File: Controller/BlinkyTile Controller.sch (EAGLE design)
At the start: 27 parts, among them IC1 74LVC1G17DCK, IC2 74LVC1G17DCK, Q1 CRYSTAL_4PAD2520, SW1 SPST_TACT-EVQQ2, SW2 SPST_TACT-EVQQ2, T1 TEST_PAD-7, T2 TEST_PAD-7, U1 MK20DX128VLF5

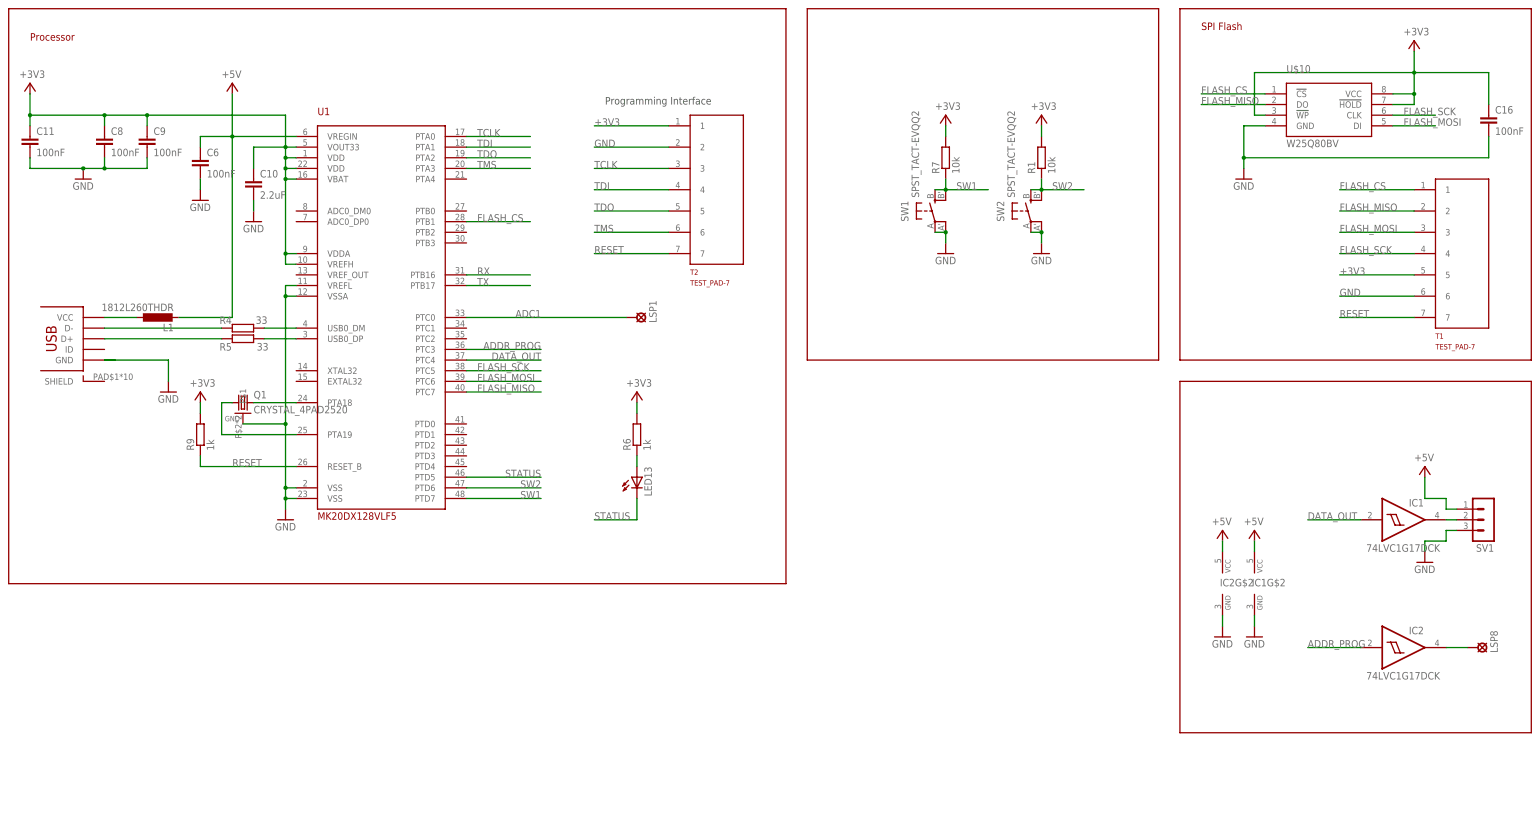
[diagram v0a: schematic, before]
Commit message: Update controller board design for RevA
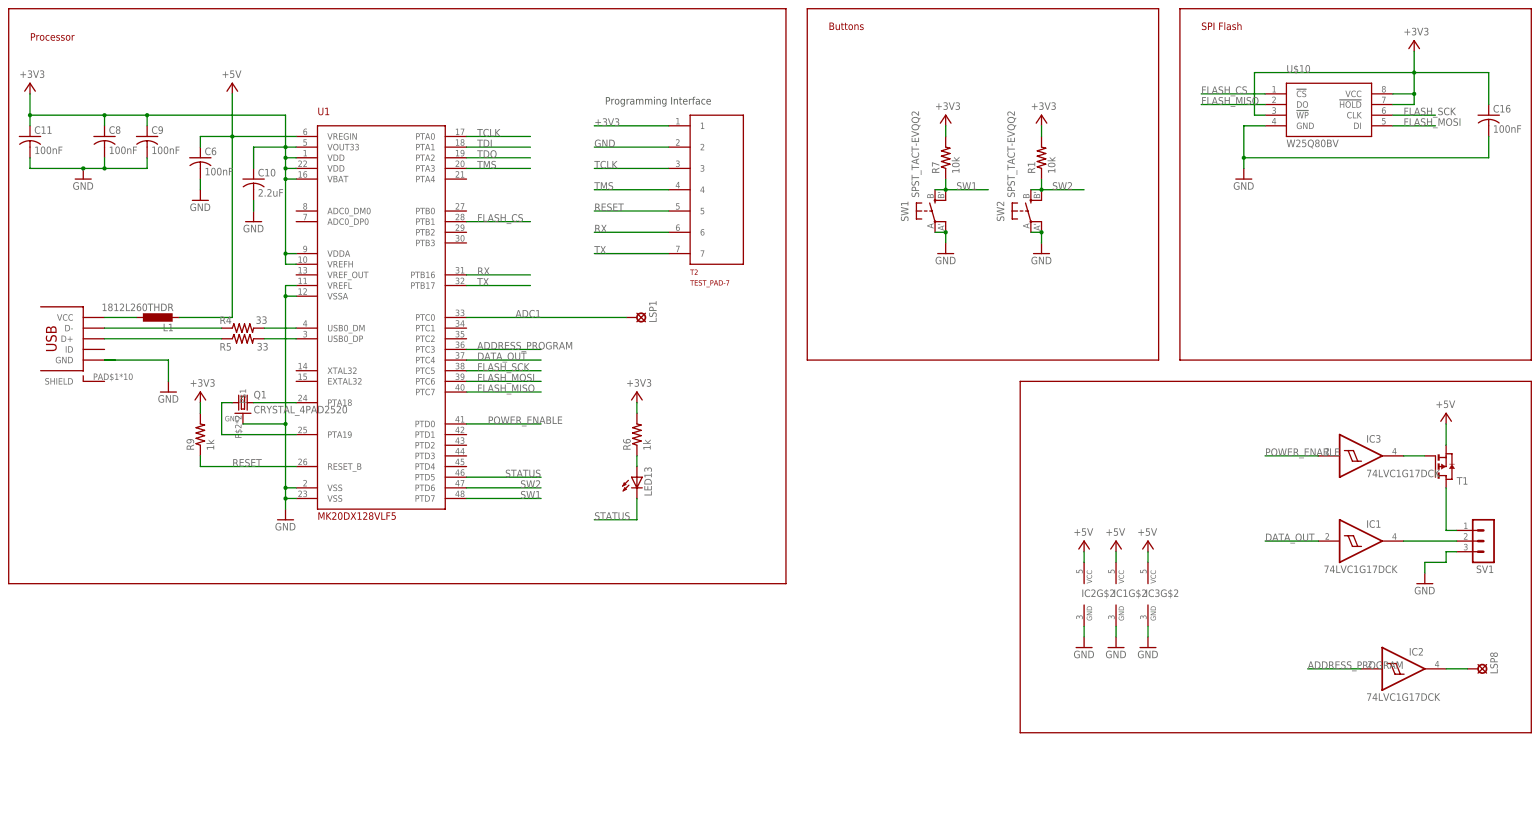
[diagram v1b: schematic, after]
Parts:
- added IC3: 74LVC1G17DCK, 74xx-little-us:74LVC1G17DCK
- C10, C11, C16, C6, C8, C9: device rcl:C-EUC0402 -> adafruit:C-USC0402
- R1, R4, R5, R6, R7, R9: device rcl:R-EU_R0402 -> adafruit:R-US_R0402
- T1: value TEST_PAD-7 -> (none); device Sam Library:TEST_PAD-7 -> zetex:PMOSSOT23
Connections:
- net ADDR_PROG renamed ADDRESS_PROGRAM
- new net N$5: SV1.1, T1.D
- new net N$6: IC3G$1.O, T1.G
- new net POWER_ENABLE: IC3G$1.I, U1.PTD0
- net +3V3: no longer T1.5
- net +5V: now also IC3G$2.VCC, T1.S; no longer SV1.1
- net FLASH_CS: no longer T1.1
- net FLASH_MISO: no longer T1.2
- net FLASH_MOSI: no longer T1.3
- net FLASH_SCK: no longer T1.4
- net GND: now also IC3G$2.GND; no longer T1.6
- net RESET: now also T2.5; no longer T1.7, T2.7
- net RX: now also T2.6
- net TDI: no longer T2.4
- net TDO: no longer T2.5
- net TMS: now also T2.4; no longer T2.6
- net TX: now also T2.7
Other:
- note added: "Buttons"
- moved on the sheet: IC1, IC1G$2, IC2, IC2G$2, LSP8, SV1

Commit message: Switch to smaller processor, change FLASH_CS to hardware CS pin
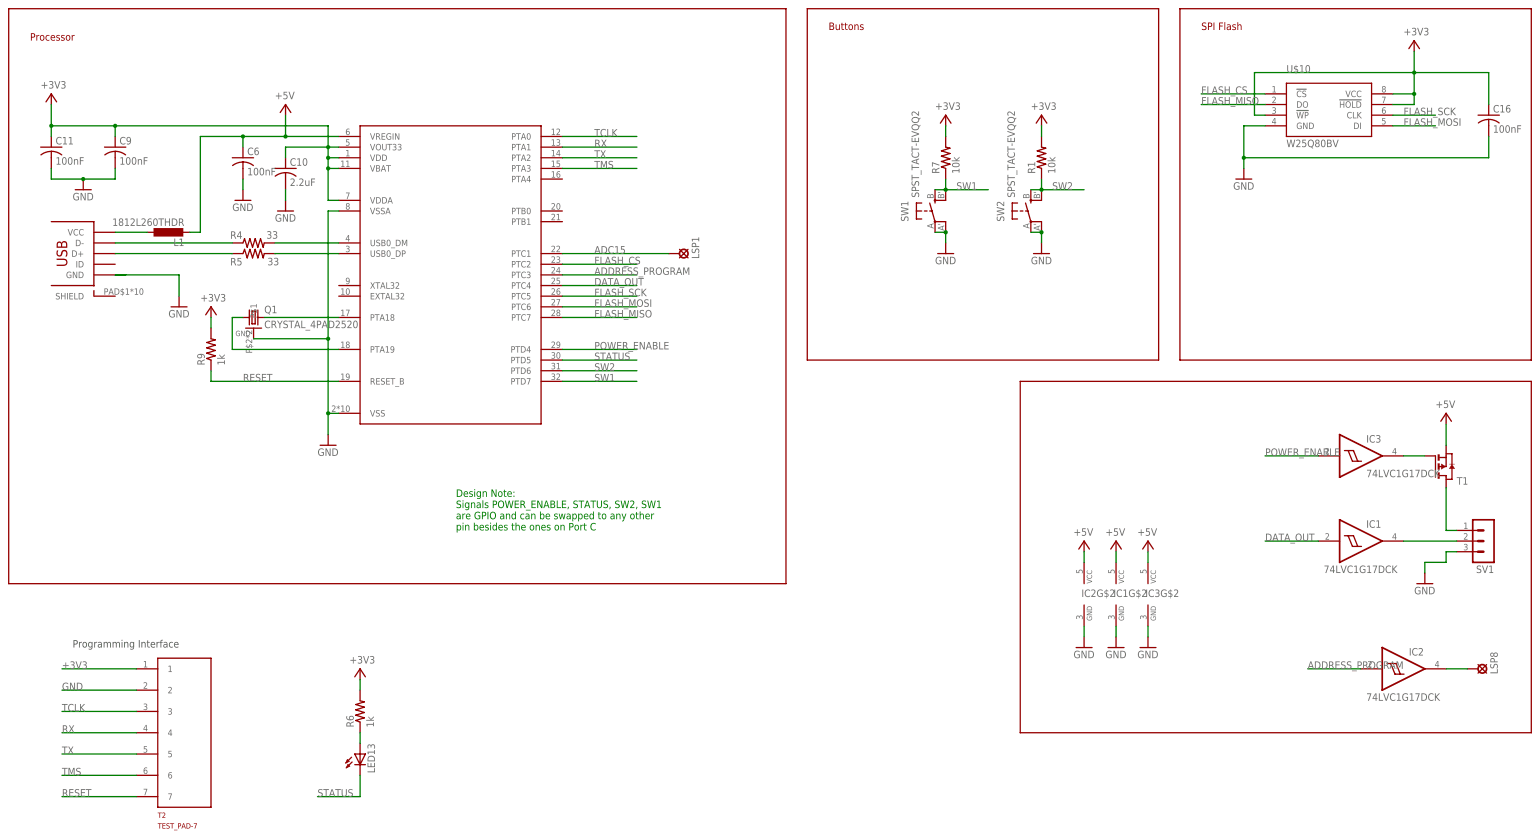
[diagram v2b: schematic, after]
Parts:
- removed C8: 100nF, adafruit:C-USC0402
- removed U1: MK20DX128VLF5, scanlime:MK20DX128VLF5
- added U$1: MK20D--VFM5, blinkinlabs:MK20D--VFM5
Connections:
- removed net ADC1: LSP1.MP, U1.PTC0
- removed net TDI: U1.PTA1
- removed net TDO: U1.PTA2
- new net ADC15: LSP1.MP, U$1.PTC1
- net +3V3: now also U$1.VBAT, U$1.VDD, U$1.VDDA, U$1.VOUT33; no longer C8.1, U1.VBAT, U1.VDD@1, U1.VDD@2, U1.VDDA, U1.VOUT33, U1.VREFH
- net +5V: now also U$1.VREGIN; no longer U1.VREGIN
- net ADDRESS_PROGRAM: now also U$1.PTC3; no longer U1.PTC3
- net DATA_OUT: now also U$1.PTC4; no longer U1.PTC4
- net FLASH_CS: now also U$1.PTC2; no longer U1.PTB1
- net FLASH_MISO: now also U$1.PTC7; no longer U1.PTC7
- net FLASH_MOSI: now also U$1.PTC6; no longer U1.PTC6
- net FLASH_SCK: now also U$1.PTC5; no longer U1.PTC5
- net GND: now also U$1.VSS, U$1.VSSA; no longer C8.2, U1.VREFL, U1.VSS@1, U1.VSS@2, U1.VSSA
- net N$1: now also U$1.PTA19; no longer U1.PTA19
- net N$11: now also U$1.USB0_DM; no longer U1.USB0_DM
- net N$12: now also U$1.USB0_DP; no longer U1.USB0_DP
- net N$2: now also U$1.PTA18; no longer U1.PTA18
- net POWER_ENABLE: now also U$1.PTD4; no longer U1.PTD0
- net RESET: now also T2.7, U$1.RESET_B; no longer T2.5, U1.RESET_B
- net RX: now also T2.4, U$1.PTA1; no longer T2.6, U1.PTB16
- net STATUS: now also U$1.PTD5; no longer U1.PTD5
- net SW1: now also U$1.PTD7; no longer U1.PTD7
- net SW2: now also U$1.PTD6; no longer U1.PTD6
- net TCLK: now also U$1.PTA0; no longer U1.PTA0
- net TMS: now also T2.6, U$1.PTA3; no longer T2.4, U1.PTA3
- net TX: now also T2.5, U$1.PTA2; no longer T2.7, U1.PTB17
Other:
- note added: "Design Note: Signals POWER_ENABLE, STATUS, SW2, SW1 are GPIO and can be swapped to any other pin besides the ones on Port C"
- moved on the sheet: C10, C11, C6, C9, L1, LED13, LSP1, Q1, R4, R5, R6, R9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

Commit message: Update to RevB controller from Sam
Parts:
- removed LED13: (no value), adafruit:LEDCHIPLED_0805
- removed R7: 10k, adafruit:R-US_R0402
- removed T2: TEST_PAD-7, Sam Library:TEST_PAD-7
- added C3: 100nF, adafruit:C-USC0402
- added CON2: F-2X04-DIL-100, con-headers-jp:F-2X04-DIL-100
- added LED1: STATUS, adafruit:LEDCHIPLED_0805
- added R2: 33, adafruit:R-US_R0402
- R1: value 10k -> 33
- R4: value 33 -> 1k
- R5: value 33 -> 10k
- R6: value 1k -> 10k
- TP1: value SE11 -> ADCIN
- TP2: value SE11 -> ADDRESS
- renumbered C10 to C4, C11 to C1, C16 to C5, C9 to C2, IC1 to U4, IC2 to U5, IC3 to U3, LSP1 to TP1, LSP8 to TP2, R9 to R3, SV1 to CON3, U$1 to U1, U$10 to U2, U$7 to CON1
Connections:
- new net PA4: CON2.8, U1.PTA4
- net +3V3: now also C6.1, CON2.1, R4.2, R5.2; no longer R1.2, R7.2, T2.1
- net +5V: now also C3.1; no longer C6.1
- net GND: now also C3.2, CON2.2; no longer T2.2
- net N$10: now also R2.1; no longer R5.1
- net N$11: now also R1.2; no longer R4.2
- net N$12: now also R2.2; no longer R5.2
- net N$16: now also LED1.A, R4.1; no longer LED13.A, R6.1
- net N$9: now also R1.1; no longer R4.1
- net RESET: now also CON2.7; no longer T2.7
- net RX: now also CON2.4; no longer T2.4
- net STATUS: now also LED1.C, U1.PTD7; no longer LED13.C, U1.PTD5
- net SW1: now also R5.1, U1.PTD6; no longer R7.1, U1.PTD7
- net SW2: now also R6.1, U1.PTD5; no longer R1.1, U1.PTD6
- net TCLK: now also CON2.3; no longer T2.3
- net TMS: now also CON2.6; no longer T2.6
- net TX: now also CON2.5; no longer T2.5
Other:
- moved on the sheet: C6, R1, R4, R5, R6

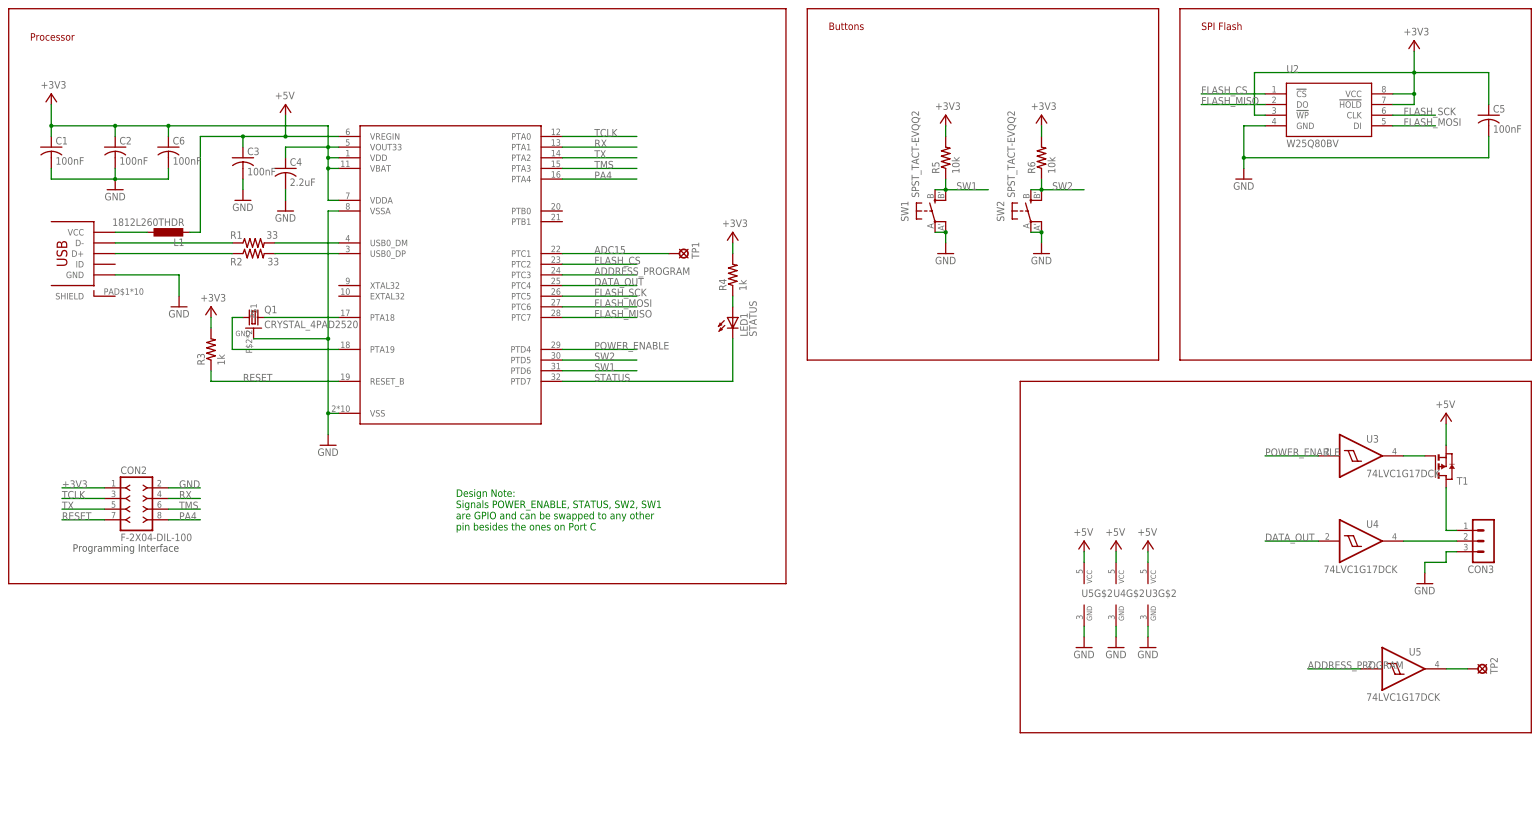
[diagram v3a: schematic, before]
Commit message: PCB updates: Drop pullup resistors, change connector
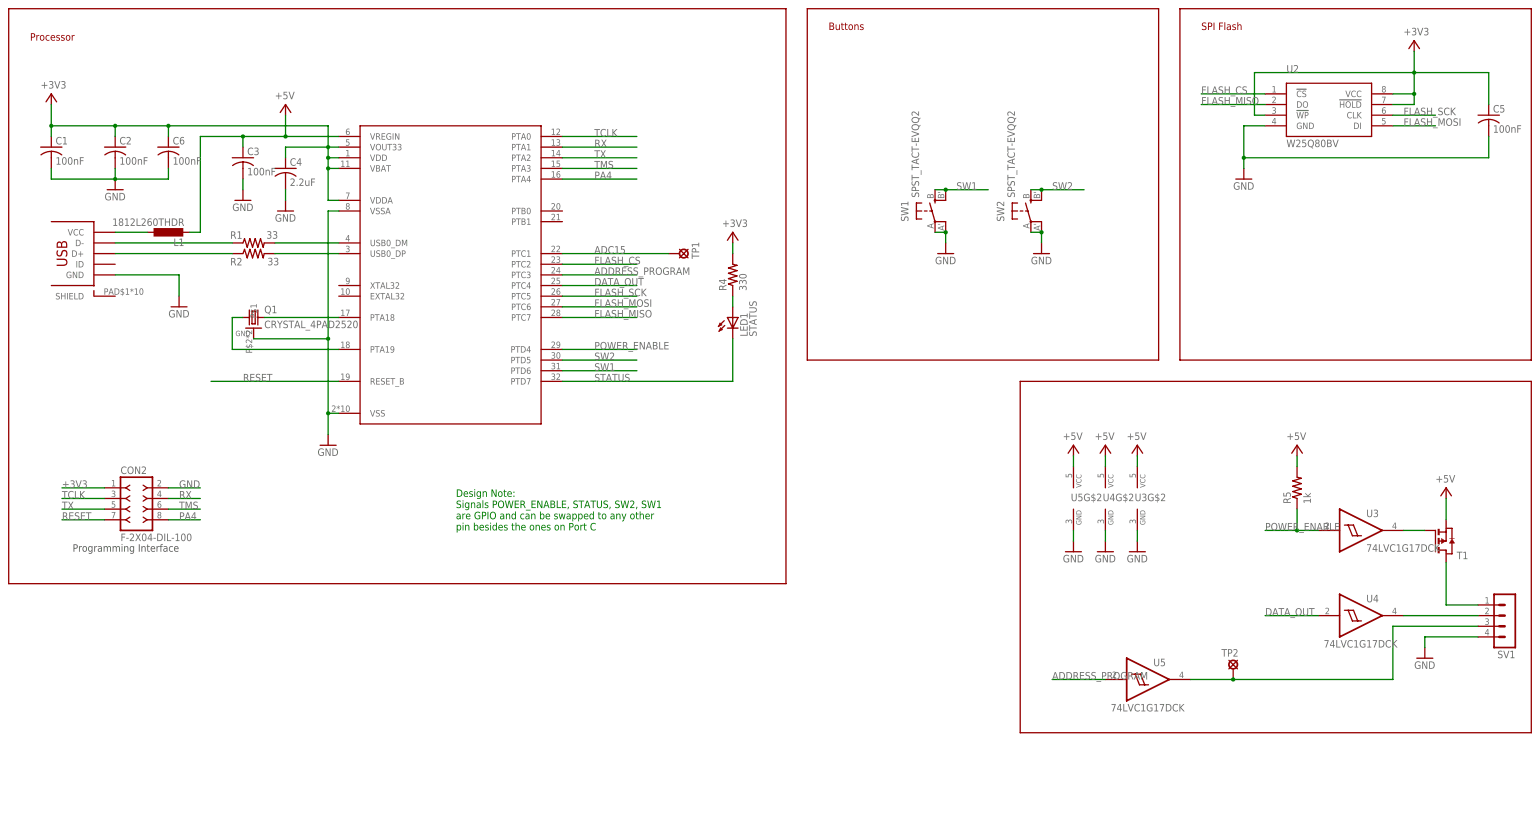
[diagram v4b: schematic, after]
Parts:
- removed CON3: (no value), con-lstb:MA03-1
- removed R3: 1k, adafruit:R-US_R0402
- removed R6: 10k, adafruit:R-US_R0402
- added SV1: (no value), con-lstb:MA04-1
- R4: value 1k -> 330
- R5: value 10k -> 1k
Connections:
- net +3V3: no longer R3.2, R5.2, R6.2
- net +5V: now also R5.2
- net GND: now also SV1.4; no longer CON3.3
- net LED_DATA: now also SV1.2; no longer CON3.2
- net N$4: now also SV1.3
- net N$5: now also SV1.1; no longer CON3.1
- net POWER_ENABLE: now also R5.1
- net RESET: no longer R3.1
- net SW1: no longer R5.1
- net SW2: no longer R6.1
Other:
- moved on the sheet: R5, T1, TP2, U3, U3G$2, U4, U4G$2, U5, U5G$2
